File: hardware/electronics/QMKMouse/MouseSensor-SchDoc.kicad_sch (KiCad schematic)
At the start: 6 parts

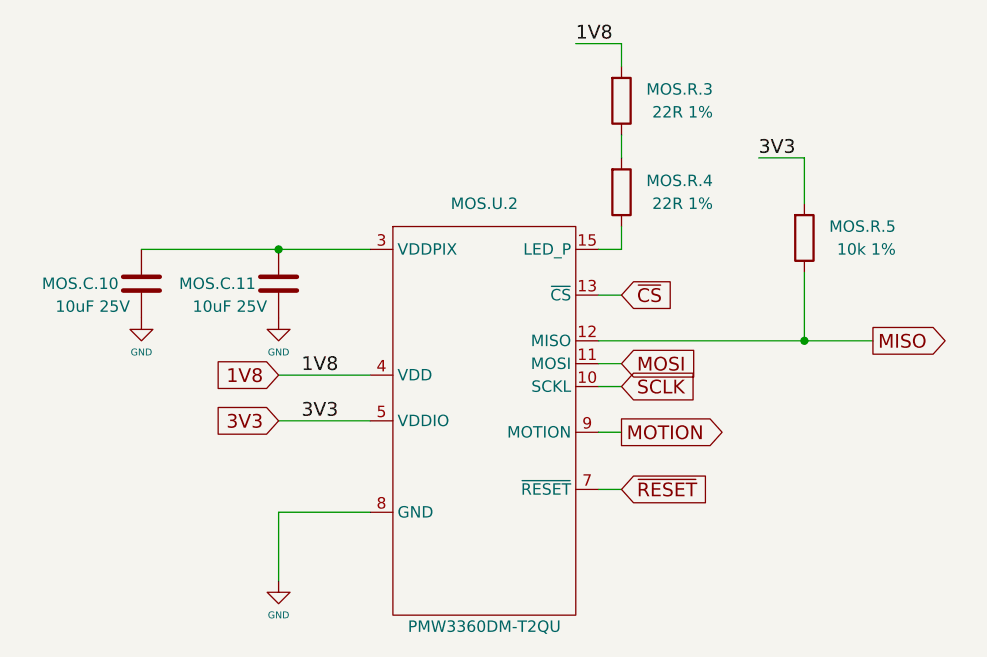
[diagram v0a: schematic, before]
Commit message: fix ERC errors and use hierarchy labels
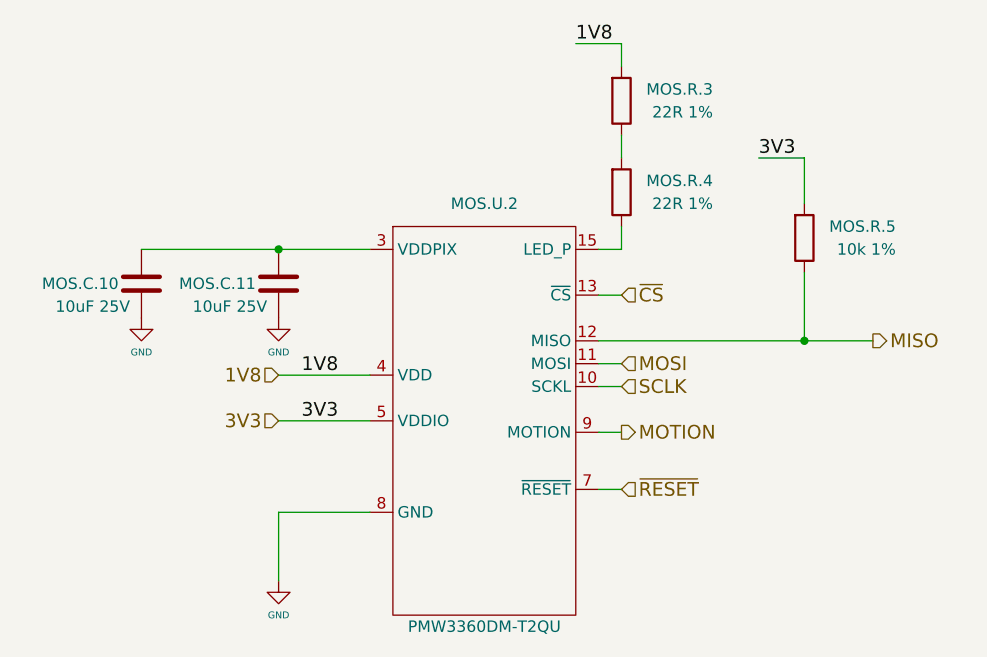
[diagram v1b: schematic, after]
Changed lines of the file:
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@@
     (effects (font (size 1.524 1.524)) (justify left bottom))
   )
-  (global_label "1V8" (shape input) (at 101.6 104.14 180) (fields_autoplaced)
+  (hierarchical_label "3V3" (shape input) (at 101.6 109.22 180)
     (effects (font (size 1.524 1.524)) (justify right))
-    (property "Intersheet References" "${INTERSHEET_REFS}" (id 0) (at 195.58 -68.58 0)
-      (effects (font (size 1.27 1.27)) (justify left) hide)
-    )
   )
-  (global_label "3V3" (shape input) (at 101.6 109.22 180) (fields_autoplaced)
+  (hierarchical_label "1V8" (shape input) (at 101.6 104.14 180)
     (effects (font (size 1.524 1.524)) (justify right))
-    (property "Intersheet References" "${INTERSHEET_REFS}" (id 0) (at 195.58 -71.12 0)
-      (effects (font (size 1.27 1.27)) (justify left) hide)
-    )
   )
-  (global_label "SCLK" (shape input) (at 139.7 105.41 0) (fields_autoplaced)
+  (hierarchical_label "MISO" (shape output) (at 167.64 100.33 0)
     (effects (font (size 1.524 1.524)) (justify left))
-    (property "Intersheet References" "${INTERSHEET_REFS}" (id 0) (at -20.32 -59.69 0)
-      (effects (font (size 1.27 1.27)) hide)
-    )
   )
-  (global_label "MISO" (shape output) (at 167.64 100.33 0) (fields_autoplaced)
+  (hierarchical_label "~{RESET}" (shape input) (at 139.7 116.84 0)
     (effects (font (size 1.524 1.524)) (justify left))
-    (property "Intersheet References" "${INTERSHEET_REFS}" (id 0) (at -22.86 -59.69 0)
-      (effects (font (size 1.27 1.27)) hide)
-    )
   )
-  (global_label "MOTION" (shape output) (at 139.7 110.49 0) (fields_autoplaced)
+  (hierarchical_label "MOTION" (shape output) (at 139.7 110.49 0)
     (effects (font (size 1.524 1.524)) (justify left))
-    (property "Intersheet References" "${INTERSHEET_REFS}" (id 0) (at -20.32 -62.23 0)
-      (effects (font (size 1.27 1.27)) hide)
-    )
   )
-  (global_label "MOSI" (shape input) (at 139.7 102.87 0) (fields_autoplaced)
+  (hierarchical_label "SCLK" (shape input) (at 139.7 105.41 0)
     (effects (font (size 1.524 1.524)) (justify left))
-    (property "Intersheet References" "${INTERSHEET_REFS}" (id 0) (at -20.32 -59.69 0)
-      (effects (font (size 1.27 1.27)) hide)
-    )
   )
-  (global_label "~{CS}" (shape input) (at 139.7 95.25 0) (fields_autoplaced)
+  (hierarchical_label "MOSI" (shape input) (at 139.7 102.87 0)
     (effects (font (size 1.524 1.524)) (justify left))
-    (property "Intersheet References" "${INTERSHEET_REFS}" (id 0) (at -20.32 -59.69 0)
-      (effects (font (size 1.27 1.27)) hide)
-    )
   )
-  (global_label "~{RESET}" (shape input) (at 139.7 116.84 0) (fields_autoplaced)
+  (hierarchical_label "~{CS}" (shape input) (at 139.7 95.25 0)
     (effects (font (size 1.524 1.524)) (justify left))
-    (property "Intersheet References" "${INTERSHEET_REFS}" (id 0) (at -20.32 -66.04 0)
-      (effects (font (size 1.27 1.27)) hide)
-    )
   )
   (symbol (lib_id "power:GND") (at 101.6 127 0) (unit 1)

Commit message: Fix capacitor value and streamline resistor value naming
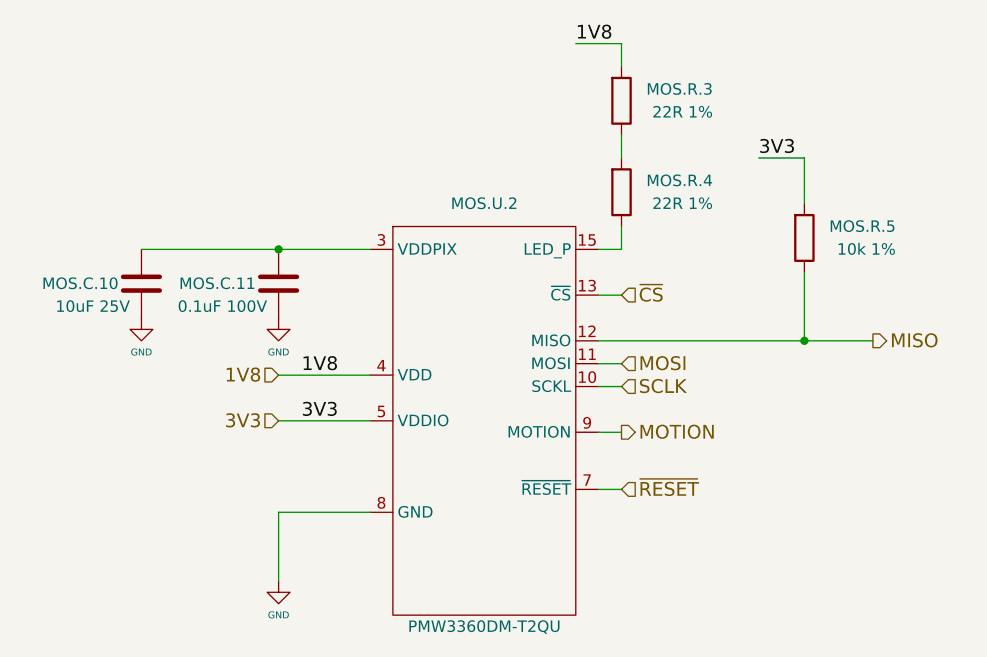
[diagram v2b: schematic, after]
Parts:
- MOS.C.11: value 10uF 25V -> 0.1uF 100V
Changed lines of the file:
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@@
       (effects (font (size 1.27 1.27)) (justify right))
     )
-    (property "Value" "10uF 25V" (id 1) (at 100.33 96.52 0)
+    (property "Value" "0.1uF 100V" (id 1) (at 100.33 96.52 0)
       (effects (font (size 1.27 1.27)) (justify right))
     )

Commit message: reference 3d model to all components
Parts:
- MOS.C.10, MOS.C.11: footprint Chip_Passives.PcbLib:0805 -> mouse_part:C_0805
- MOS.R.3, MOS.R.4, MOS.R.5: footprint Chip_Passives.PcbLib:0805 -> mouse_part:0805
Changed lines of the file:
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@@
       (effects (font (size 1.27 1.27)) (justify right))
     )
-    (property "Footprint" "Chip_Passives.PcbLib:0805" (id 2) (at 137.922 83.82 90)
+    (property "Footprint" "mouse_part:0805" (id 2) (at 137.922 83.82 90)
       (effects (font (size 1.27 1.27)) hide)
     )
@@
       (effects (font (size 1.27 1.27)) (justify right))
     )
-    (property "Footprint" "Chip_Passives.PcbLib:0805" (id 2) (at 158.242 88.9 90)
+    (property "Footprint" "mouse_part:0805" (id 2) (at 158.242 88.9 90)
       (effects (font (size 1.27 1.27)) hide)
     )
@@
       (effects (font (size 1.27 1.27)) (justify right))
     )
-    (property "Footprint" "Chip_Passives.PcbLib:0805" (id 2) (at 102.5652 90.17 0)
+    (property "Footprint" "mouse_part:C_0805" (id 2) (at 102.5652 90.17 0)
       (effects (font (size 1.27 1.27)) hide)
     )
@@
       (effects (font (size 1.27 1.27)) (justify right))
     )
-    (property "Footprint" "Chip_Passives.PcbLib:0805" (id 2) (at 87.3252 90.17 0)
+    (property "Footprint" "mouse_part:C_0805" (id 2) (at 87.3252 90.17 0)
       (effects (font (size 1.27 1.27)) hide)
     )
@@
       (effects (font (size 1.27 1.27)) (justify right))
     )
-    (property "Footprint" "Chip_Passives.PcbLib:0805" (id 2) (at 137.922 73.66 90)
+    (property "Footprint" "mouse_part:0805" (id 2) (at 137.922 73.66 90)
       (effects (font (size 1.27 1.27)) hide)
     )
